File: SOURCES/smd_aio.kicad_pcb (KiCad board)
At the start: 2 copper layers, 159.8 x 99.8 mm, 209 parts, among them J1 RCA_01, J2 RCA_01, J3 RCA_01, J4 RCA_01, P1 MUTE, P10 CONN_01X02, P11 FCR684205T, P12 FCR684205R, P13 CONN_01X02, P14 CONN_01X02, P15 CONN_01X02, P16 TST, P17 MC4, P18 TST, P19 TST, P2 CONN_01X04, P20 TST, P21 TST, P22 TST, P23 TST, P24 MP11, P25 MP6, P26 MP10, P27 TST, P28 TST, P29 TST, P3 CONN_01X03, P30 TST, P31 CONN_01X03, P32 /SD, P33 GP4, P34 GP5, P35 GP6, P4 CONN_02X05 Boxed, P5 STDCONN, P6 CONN_02X04, P7 CONN_02X04, P8 CONN_02X04, P9 CONN_01X02, SW1 SW_PUSH, T1 Transformer_1P_1S_DA101JC, T2 Transformer_1P_1S_DA101JC, U1 ADAU1701, U10 IDT2309NZ, U11 LM1117MP-1.8, U12 LM1117MP-3.3, U2 24AA256SN, U3 SN74LVC14ADG4, U4 TAS5760MDCAR, U5 CS8422, U6 CS8406-CZZ, U7 LM2842Y, U8 MCP23008, U9 TAS5760MDCAR, X1 ASV-24.576MHz-EJ-T

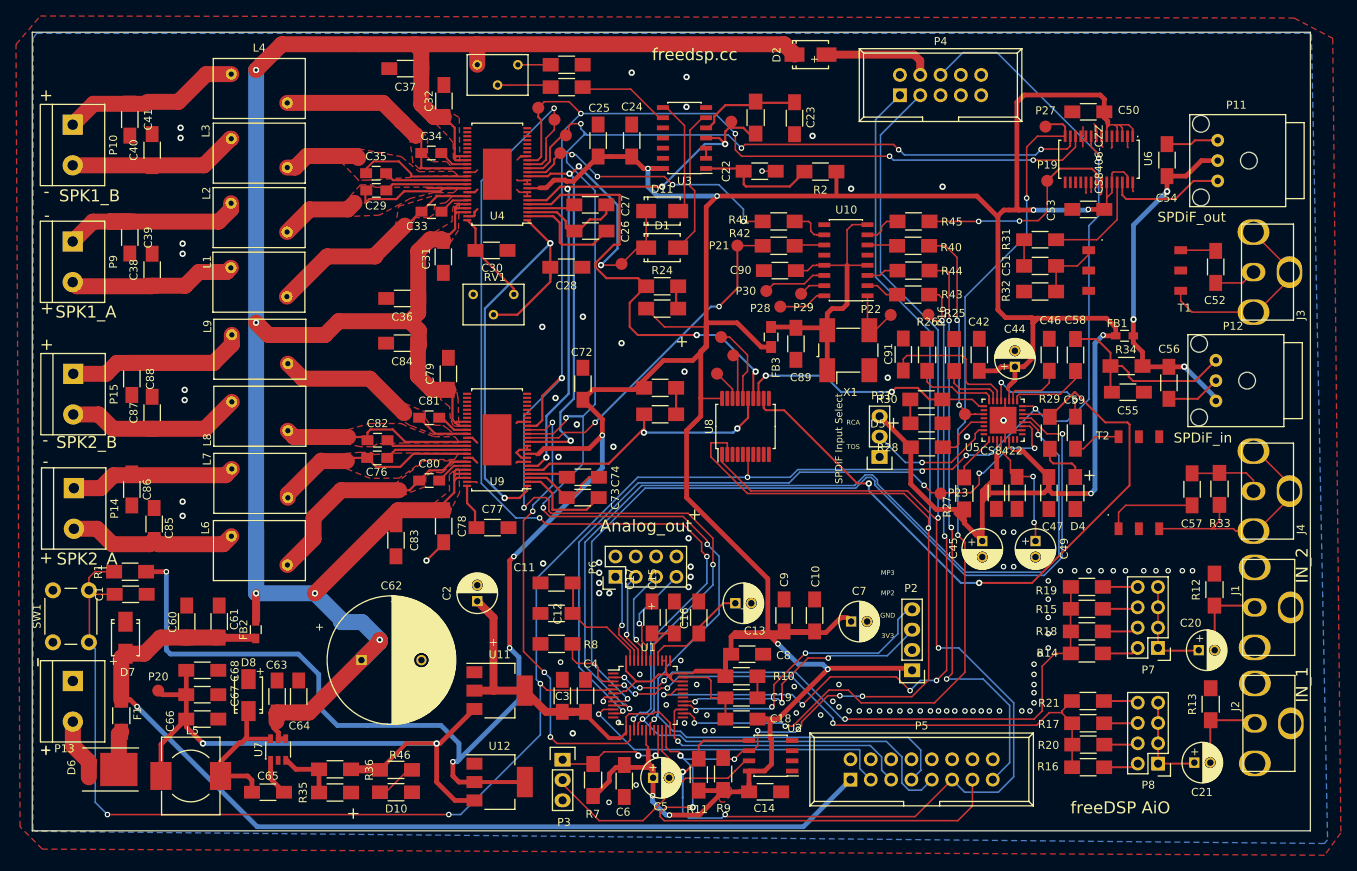
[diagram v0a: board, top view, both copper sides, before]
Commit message: Moved input cap and Reset btn.
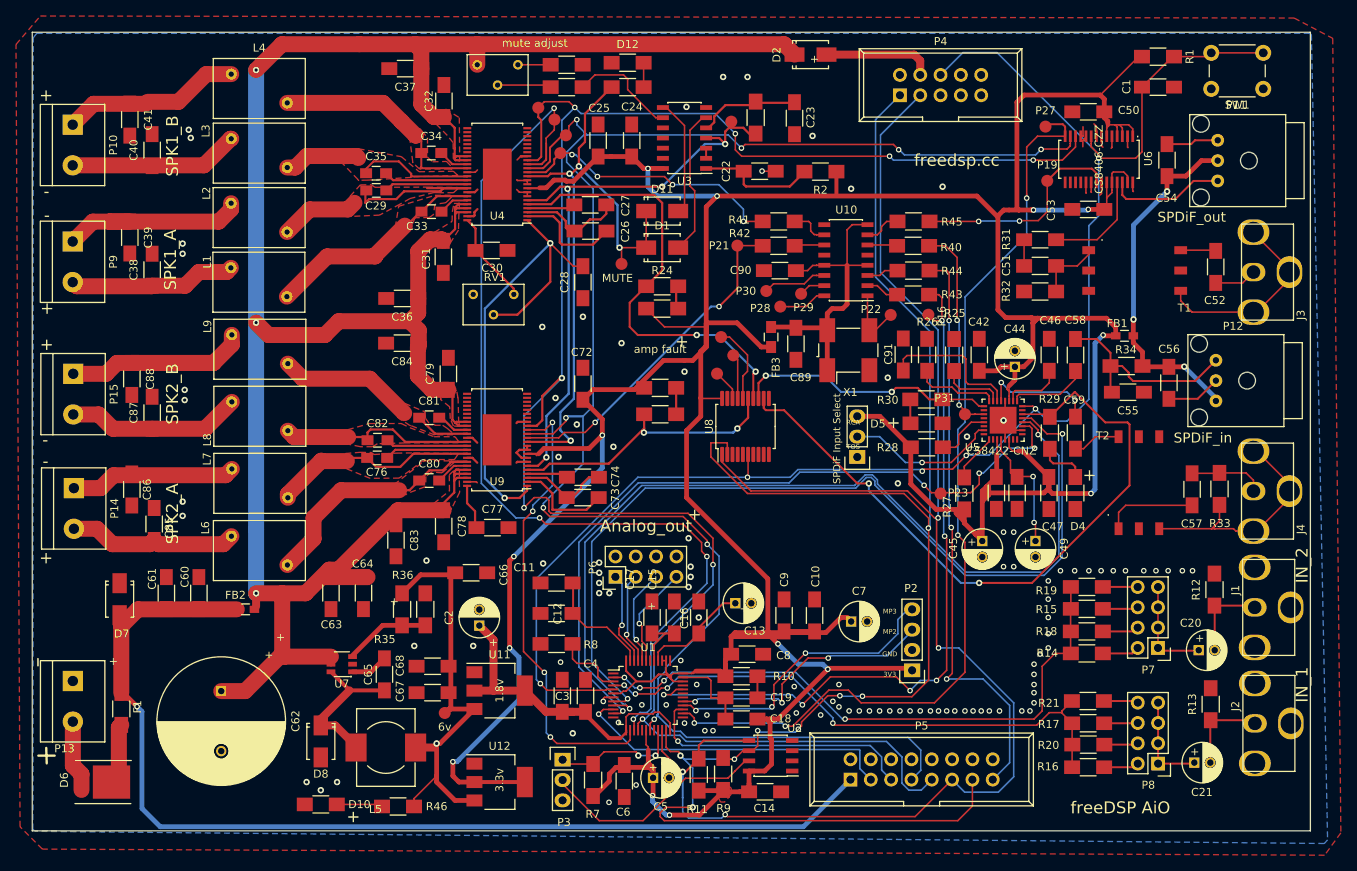
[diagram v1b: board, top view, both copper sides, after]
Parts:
- added D12: LED_RED, fdsp_resistor:R_1206_HandSoldering, F.Cu at (93.2, 20.8)
- added R6: 1k, fdsp_resistor:R_1206_HandSoldering, F.Cu at (93.2, 23.9)
- C62: value 100u -> 2200u
- U3: value SN74LVC14ADG4 -> 7414
- U5: value CS8422 -> CS8422-CNZ
- U8: value MCP23008 -> MCP23008-xSS
- moved SW1 166.4 mm to (172.7, 24.1), turned to 180 degrees
- moved R1 143.7 mm to (159.5, 20.1), turned to 0 degrees
- moved C1 143.2 mm to (159.5, 23.9)
- moved C66 38.3 mm to (73.7, 84.6)
- moved 6v 35.9 mm to (70.4, 102.1), turned to 180 degrees
- moved C68 28.8 mm to (68.8, 96.3), turned to 180 degrees
- moved C67 28.8 mm to (68.8, 99.6), turned to 180 degrees
- moved R35 25.5 mm to (67.9, 89.2), turned to 90 degrees
- moved L5 24.6 mm to (63.0, 106.4), turned to 0 degrees
- moved R36 21.7 mm to (65.0, 89.2), turned to -90 degrees
- moved C65 20.7 mm to (62.8, 97.3), turned to 90 degrees
- moved C62 17.9 mm to (42.4, 99.4), turned to -90 degrees
- moved C64 15.3 mm to (60.2, 87.1), turned to -90 degrees
- moved C63 14.6 mm to (56.1, 87.1), turned to -90 degrees
- moved U7 13.3 mm to (57.5, 96.0), turned to 180 degrees
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- renumbered P20 to 6v
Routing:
- net BRD_RST: track 269.8 -> 198.5 mm, vias 8 -> 6
- net +3V3: track 653.6 -> 605.5 mm, vias 15 -> 14
- net +6V: track 79.9 -> 52.5 mm, vias 2 -> 1
- net VCC: track 304.8 -> 288.2 mm, vias 5 -> 3
- net VIN: track 123.3 -> 131.3 mm
- net SPK_SLEEP: track 73.6 -> 81.2 mm
- net SFT_CLIP: track 59.2 -> 63.0 mm
- net GND: track 62.2 -> 59.0 mm, vias 103 -> 115
- net +1V8: track 43.1 -> 39.9 mm
- net /Power/lm-fb: track 7.53 -> 10.6 mm
- net Net-(D12-A): track 0.00 -> 3.05 mm
- net Net-(D6-K): track 4.85 -> 7.65 mm
- net RX_SEL: track 16.4 -> 19.2 mm
- net Net-(U3-4A): track 11.6 -> 13.6 mm
- net +12V: track 7.79 -> 8.99 mm
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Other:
- board text added: "1.8v"
- board text added: "3.3v"
- board text added: "amp fault"
- board text added: "mute adjust"

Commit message: Added mute adjust, improved layout.
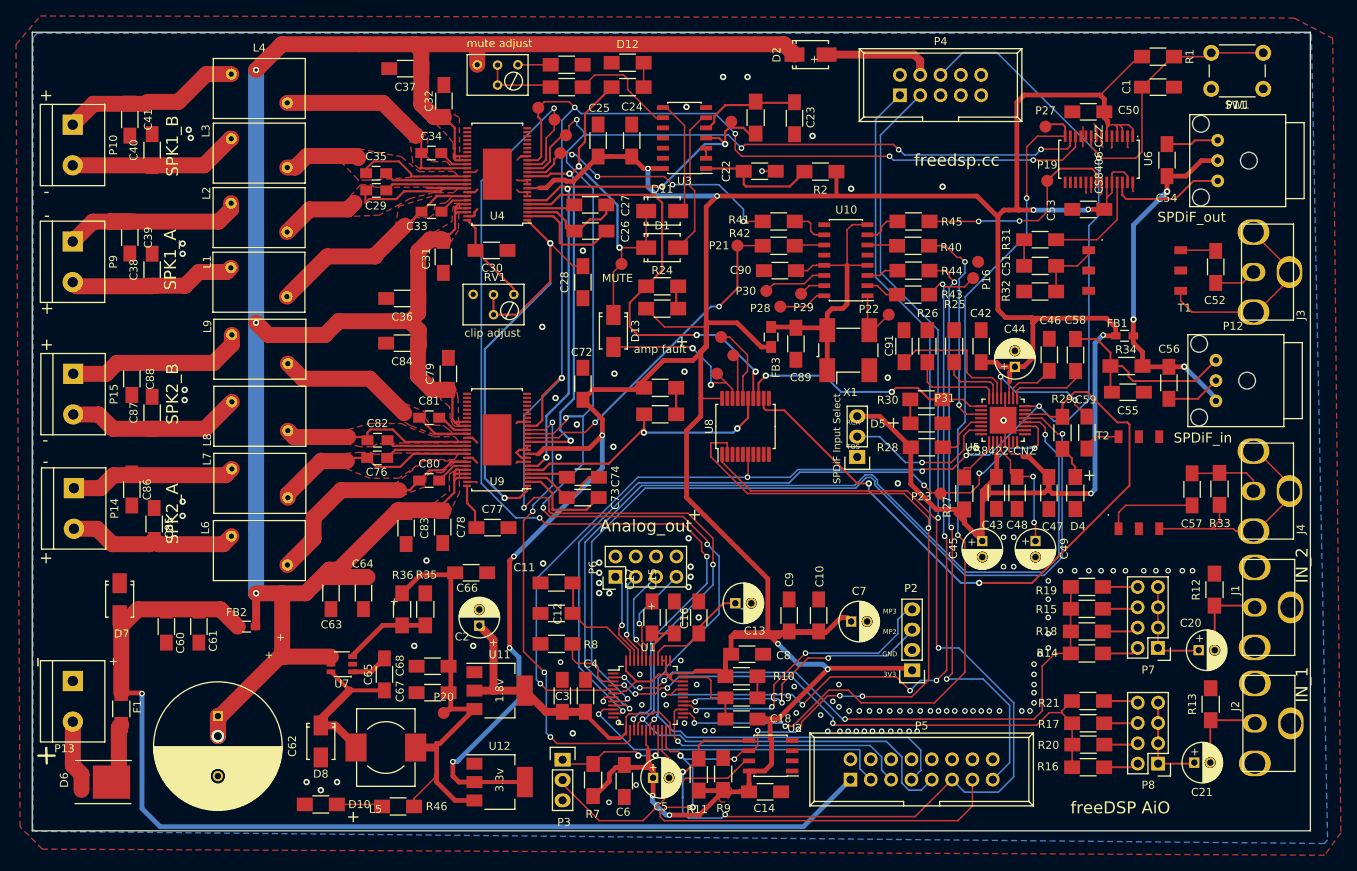
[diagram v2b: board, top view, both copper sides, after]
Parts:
- removed 6v: TST, fdsp_misc:Measurement_Point_Round-SMD-Pad_Small
- added D13: B150, fdsp_diode:SMA, F.Cu at (91.4, 54.4)
- added P20: TST, fdsp_misc:Measurement_Point_Round-SMD-Pad_Small, F.Cu at (70.2, 102.1)
- C62: value 2200u -> 100u
- U3: value 7414 -> SN74LVC14ADG4
- moved P18 19.1 mm to (137.0, 45.7)
- moved P16 7.22 mm to (136.4, 47.8)
- moved C60 5.84 mm to (35.6, 91.3), turned to -90 degrees
- moved C61 5.84 mm to (39.6, 91.3), turned to -90 degrees
- moved C62 3.15 mm to (42.0, 102.5)
- moved FB2 2.16 mm to (45.6, 91.3)
- moved C83 1.98 mm to (65.5, 79.0)
- moved R29 1.57 mm to (147.6, 67.1)
- moved C59 1.42 mm to (150.6, 67.1)
- moved C42 1.10 mm to (137.4, 56.3)
- moved R25 1.10 mm to (134.0, 56.3)
- moved R26 1.08 mm to (130.7, 56.3)
- moved C91 1.04 mm to (127.8, 56.3)
- moved C9 0.64 mm to (113.4, 89.9)
- moved C10 0.51 mm to (117.1, 89.9)
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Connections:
- net Net-(U8-GP6) renamed /EXT_MUTE
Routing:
- net /EXT_MUTE: track 3.90 -> 21.4 mm, vias 0 -> 2
- net VCC: track 288.2 -> 297.5 mm, vias 3 -> 4
- net SPK_SLEEP: track 81.2 -> 88.0 mm
- net MCLK0: track 92.3 -> 96.9 mm
- net +3V3: track 605.5 -> 602.5 mm
- net SFT_CLIP: track 63.0 -> 65.5 mm
- net Net-(R5-Pad2): track 6.64 -> 9.14 mm
- net VIN: track 131.3 -> 133.6 mm
- net Net-(D4-A): track 6.22 -> 4.19 mm
- net SPDIF_IN_RCA: track 14.6 -> 15.9 mm
- net Net-(T2-PM): track 6.01 -> 4.81 mm
- net Net-(U5-MS_SEL): track 10.5 -> 11.7 mm
- net GND: track 59.0 -> 60.1 mm, vias 115 -> 126
- net Net-(U5-RXN0): track 7.58 -> 6.66 mm
- net Net-(J2-SIG): track 11.9 -> 11.0 mm
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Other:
- rule pad_to_mask_clearance: 0.2 -> 0
- board text added: "clip adjust"

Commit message: Removed old files.
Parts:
- FB2: value BLM18PG471SN1 -> BLM18SG700TZ1D
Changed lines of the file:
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@@
         (effects (font (size 1 1) (thickness 0.15)))
     )
-    (fp_text value "BLM18PG471SN1" (at 0 1.9) (layer "F.Fab")
+    (fp_text value "BLM18SG700TZ1D" (at 0 1.9) (layer "F.Fab")
         (effects (font (size 1 1) (thickness 0.15)))
     )

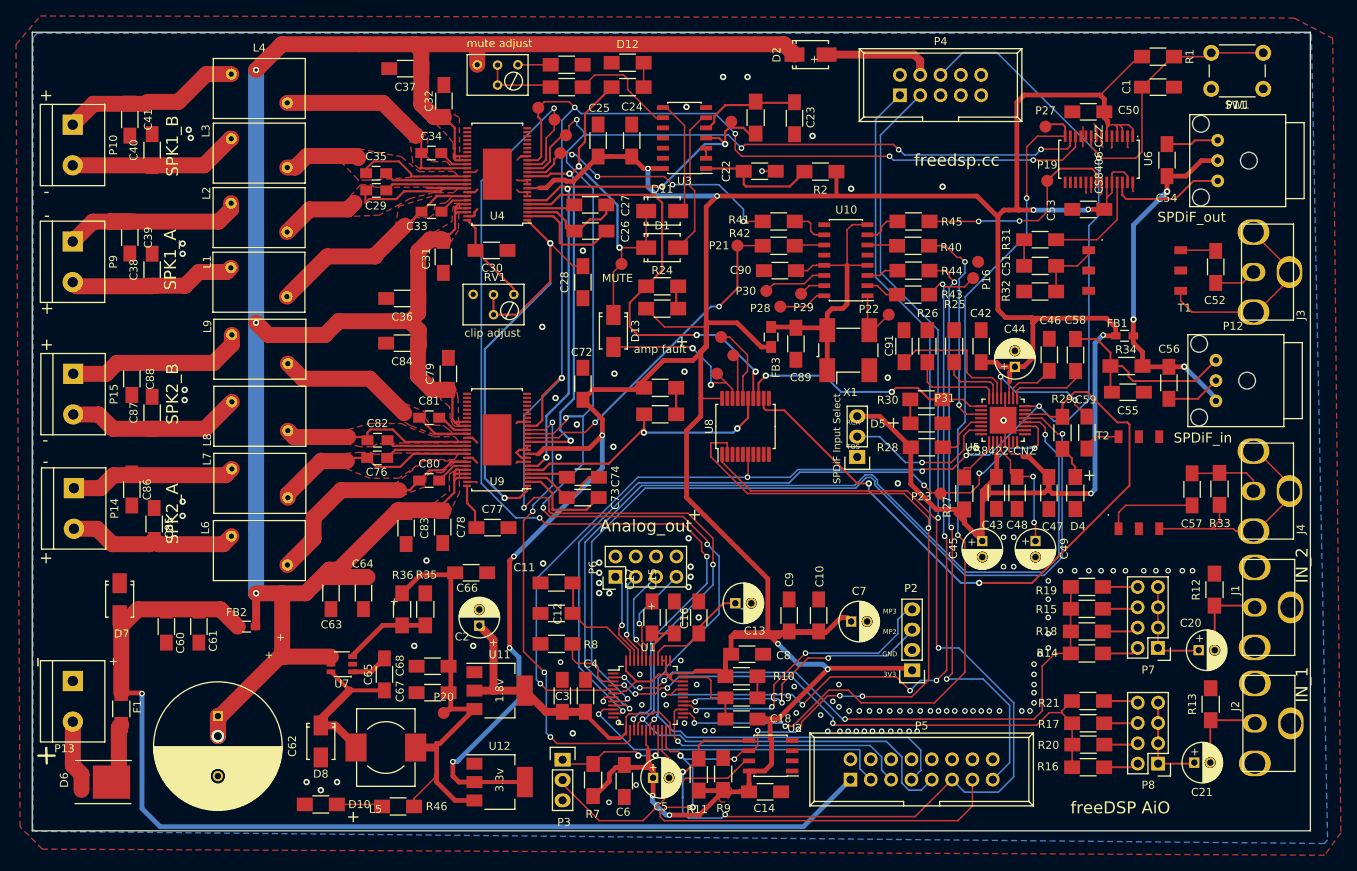
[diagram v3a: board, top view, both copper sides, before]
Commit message: Optimized Vreg traces.
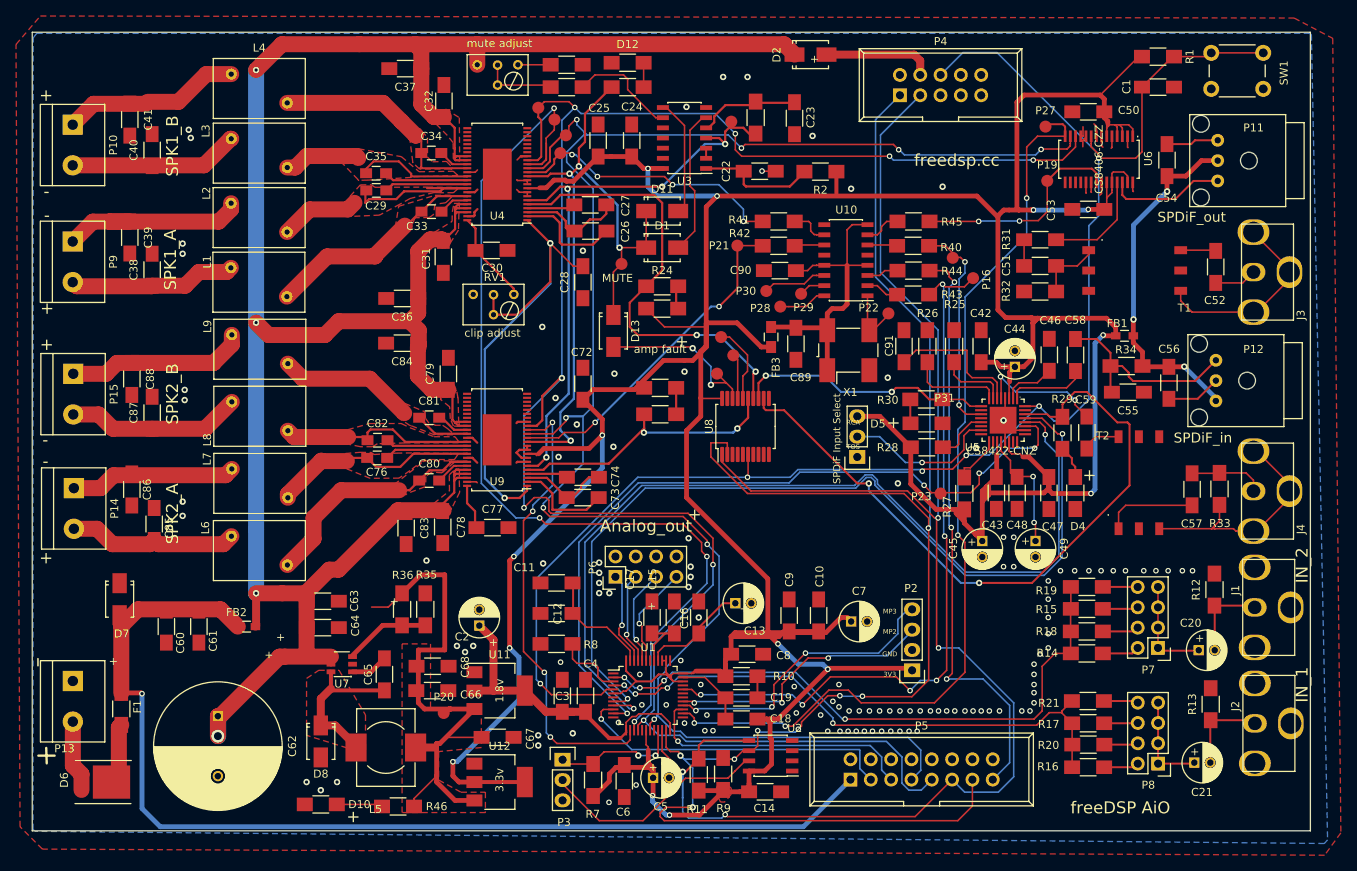
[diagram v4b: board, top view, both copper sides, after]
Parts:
- FB2: value BLM18SG700TZ1D -> BLM18PG471SN1
- moved C66 15.5 mm to (68.8, 99.3)
- moved C67 9.86 mm to (77.0, 105.2), turned to 0 degrees
- moved C64 6.67 mm to (55.1, 91.4), turned to 0 degrees
- moved P18 3.22 mm to (133.9, 45.2)
- moved C63 1.44 mm to (55.1, 88.1), turned to 0 degrees
- moved P22 0.17 mm to (125.8, 52.2)
- turned C68 to 0 degrees
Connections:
- net Net-(D8-K) renamed /Power/reg-sw
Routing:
- net +6V: track 52.5 -> 68.7 mm
- net MCLK0: track 96.9 -> 92.1 mm
- net VCC: track 297.5 -> 293.7 mm
- net GND: track 60.1 -> 58.4 mm, vias 126 -> 128
- net Net-(U1-PLL_LF): track 10.3 -> 9.03 mm
- net MP0: track 93.8 -> 94.8 mm
- net MP5: track 113.9 -> 114.8 mm
- net MP6: track 118.8 -> 118.2 mm
- net +1V8: track 39.9 -> 39.4 mm
- added copper zone on F.Cu, net +6V
- added copper zone on F.Cu, net /Power/reg-sw

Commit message: Added HP amp
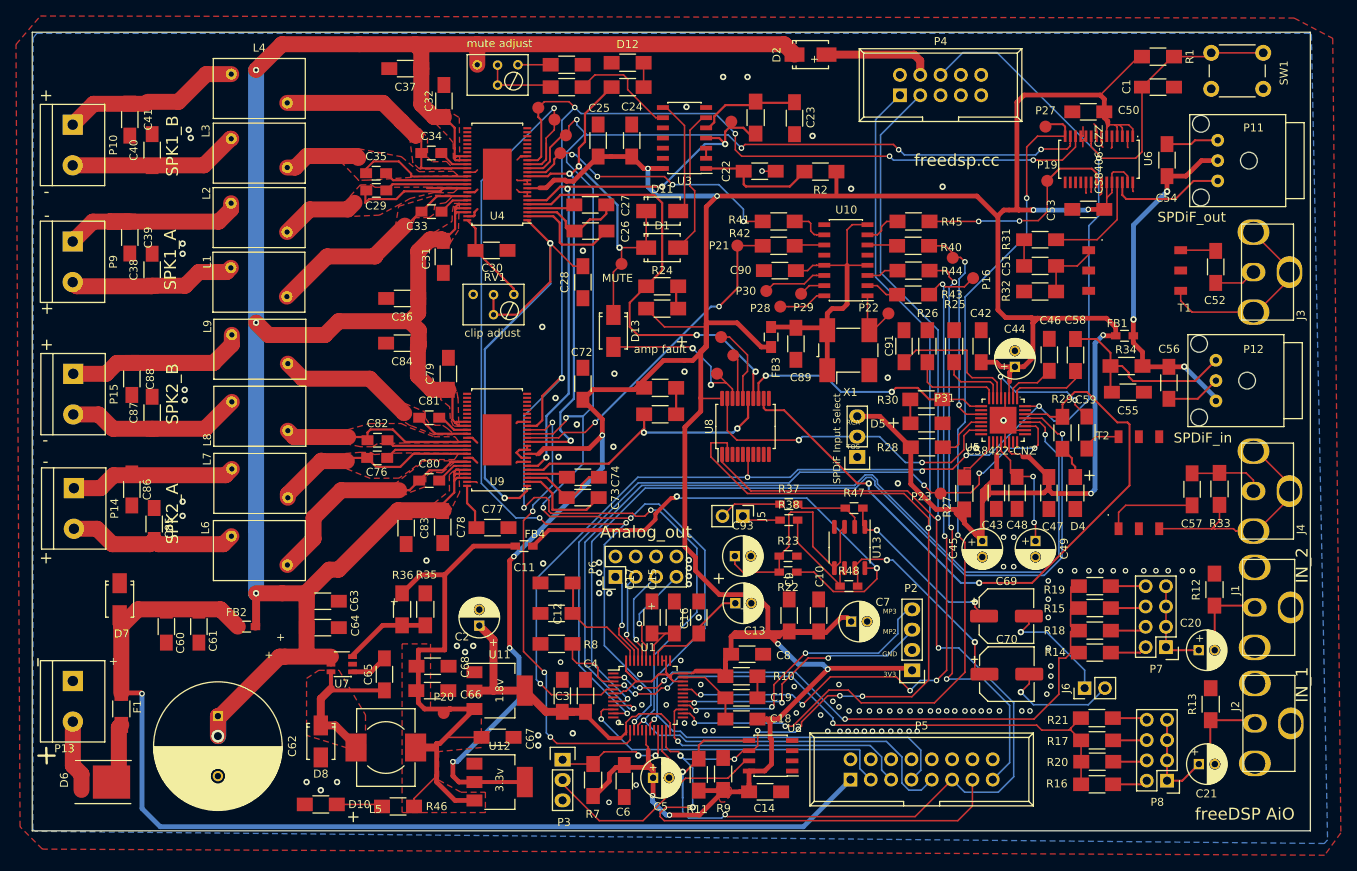
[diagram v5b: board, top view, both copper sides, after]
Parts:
- added C69: 220u, Capacitor_SMD:CP_Elec_6.3x5.9, F.Cu at (140.6, 90.0)
- added C70: 220u, Capacitor_SMD:CP_Elec_6.3x5.9, F.Cu at (140.6, 97.2)
- added C93: 10u, fdsp_capacitor:C_Radial_D5_L11_P2, F.Cu at (106.6, 82.5)
- added FB4: BLM18PG471SN1, fdsp_resistor:R_0603_HandSoldering, F.Cu at (80.3, 81.2)
- added J5: Conn_01x02, Connector_PinHeader_2.54mm:PinHeader_1x02_P2.54mm_Vertical, F.Cu at (107.6, 77.5)
- added J6: Conn_01x02, Connector_PinHeader_2.54mm:PinHeader_1x02_P2.54mm_Vertical, F.Cu at (150.3, 99.0)
- added R22: 100k, fdsp_resistor:R_0603_HandSoldering, F.Cu at (113.3, 84.5)
- added R23: 100k, fdsp_resistor:R_0603_HandSoldering, F.Cu at (113.3, 82.5)
- added R37: 2.2k, fdsp_resistor:R_0603_HandSoldering, F.Cu at (113.4, 76.0)
- added R38: 2.2k, fdsp_resistor:R_0603_HandSoldering, F.Cu at (113.4, 78.0)
- added R47: 2.2k, fdsp_resistor:R_0603_HandSoldering, F.Cu at (121.5, 76.5)
- added R48: 2.2k, fdsp_resistor:R_0603_HandSoldering, F.Cu at (120.9, 86.2)
- added U13: OP279, Package_SO:SO-8_3.9x4.9mm_P1.27mm, F.Cu at (121.0, 81.4)
- moved P8 2.41 mm to (160.6, 110.6)
- moved R16 2.41 mm to (151.9, 111.0)
- moved R17 2.41 mm to (151.9, 105.5)
- moved R20 2.41 mm to (151.9, 108.2)
- moved R21 2.41 mm to (151.9, 102.8)
- moved P7 1.00 mm to (160.5, 93.9)
- moved R14 1.00 mm to (151.6, 94.6)
- moved R15 1.00 mm to (151.6, 89.0)
- moved R18 1.00 mm to (151.6, 91.8)
- moved R19 1.00 mm to (151.6, 86.2)
- moved C21 0.60 mm to (164.6, 108.5)
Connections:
- U8 pad 19: /RX_SEL -> RX_SEL
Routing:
- net Net-(U13C-V+): track 0.00 -> 64.2 mm, vias 0 -> 2
- net Net-(U13A-+): track 0.00 -> 31.6 mm
- net Net-(C70-Pad1): track 0.00 -> 27.4 mm, vias 0 -> 2
- net Net-(C69-Pad1): track 0.00 -> 22.3 mm, vias 0 -> 2
- net RX_SEL: track 19.5 -> 40.5 mm, vias 1 -> 2
- net Net-(J6-Pin_2): track 0.00 -> 14.7 mm, vias 0 -> 1
- net Net-(J6-Pin_1): track 0.00 -> 14.6 mm, vias 0 -> 1
- net Net-(U13B--): track 0.00 -> 12.9 mm
- net Net-(U13A--): track 0.00 -> 9.00 mm
- net Net-(J5-Pin_2): track 0.00 -> 7.81 mm
- net MP6: track 118.2 -> 110.7 mm
- net +6V: track 68.7 -> 74.4 mm
- net Net-(J5-Pin_1): track 0.00 -> 4.86 mm
- net MP10: track 240.3 -> 237.3 mm
- net +3V3: track 602.5 -> 605.3 mm
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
